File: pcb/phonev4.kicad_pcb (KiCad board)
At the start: 2 copper layers, 88.9 x 124.5 mm, 44 parts, among them J1 coin, J2 keypad, J3 display, J4 RJ9, J5 mic, J6 card_reader, J7 speaker, Q1 Si2319CDS, U2 TDA2822M

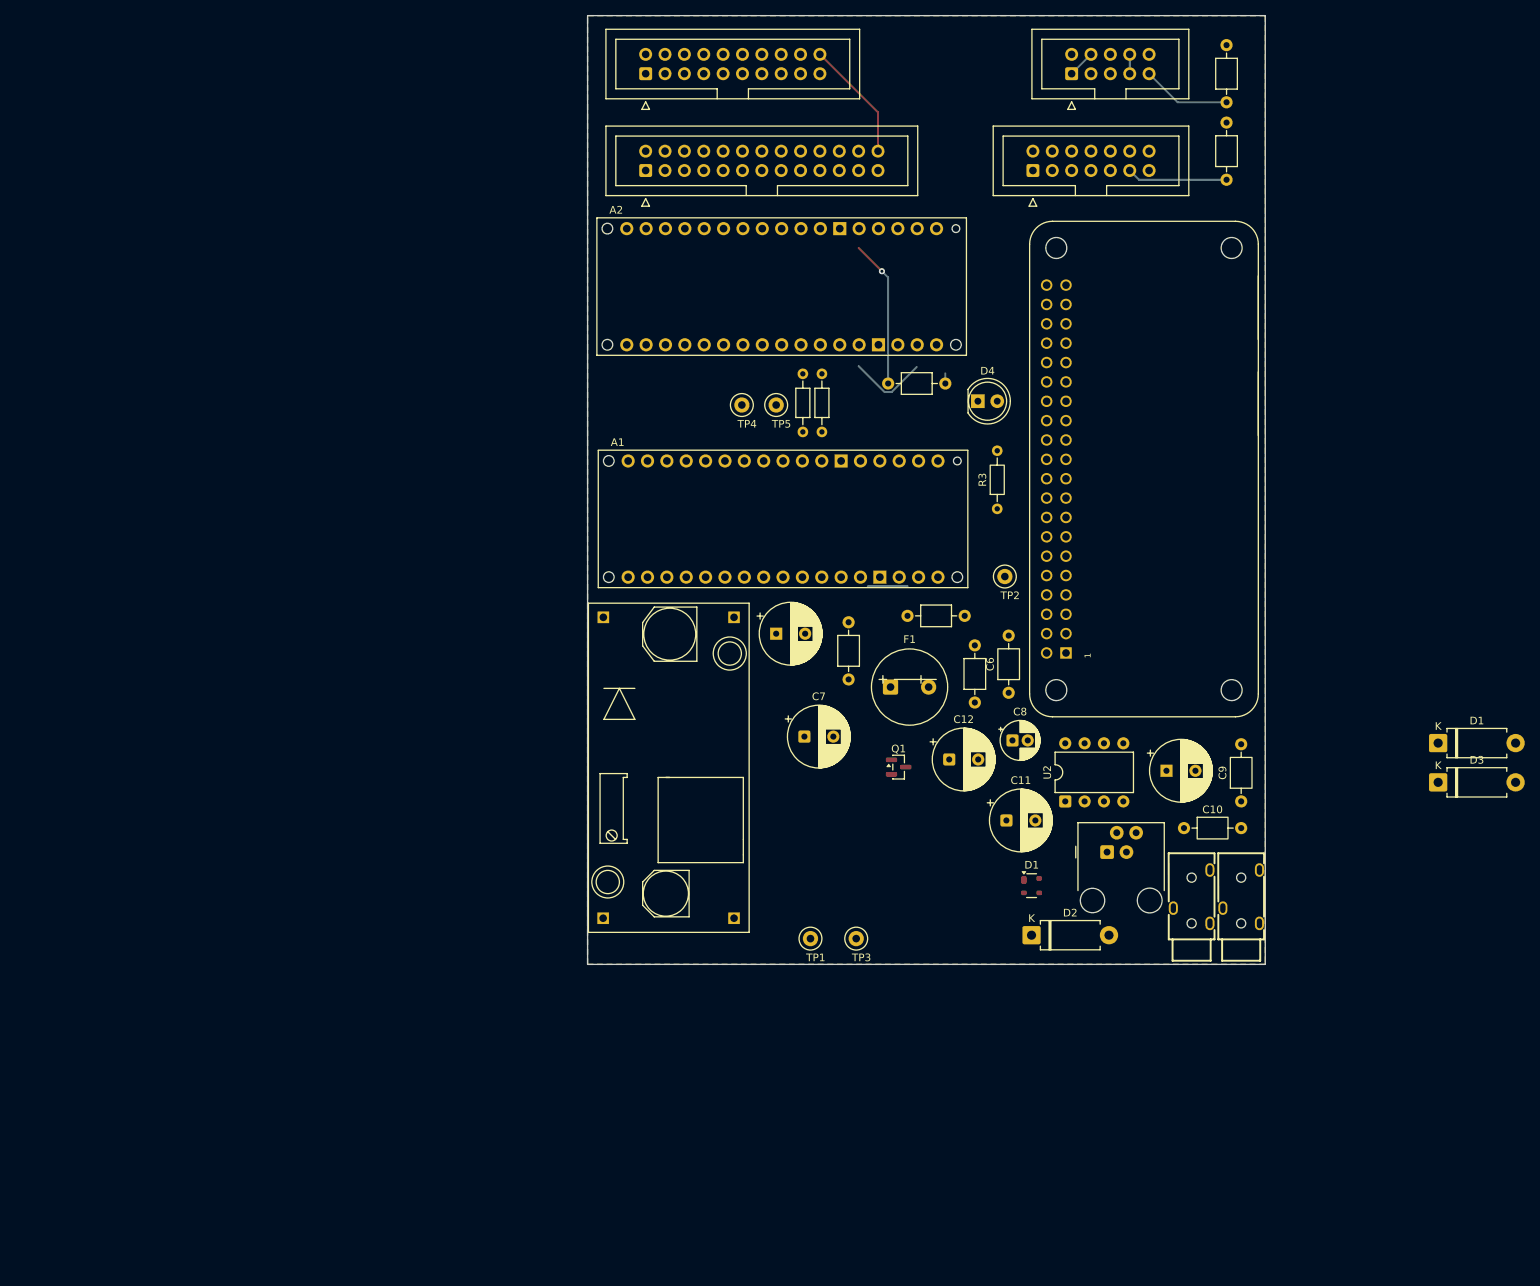
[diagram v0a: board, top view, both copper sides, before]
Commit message: pcb: phonev4 KiCad design with project footprint libraries
- Add project-local footprint libs: ADA3708, audio, PCM_arduino-library, misc_footprints
- Q1 THT: TO-220-3_Vertical_GSD for IRF9540N
- R4, R5: 1k for Pi→Arduino reset (unconnected in schematic)
- Updated fp-lib-table, BOM, README, audit script

Made-with: Cursor
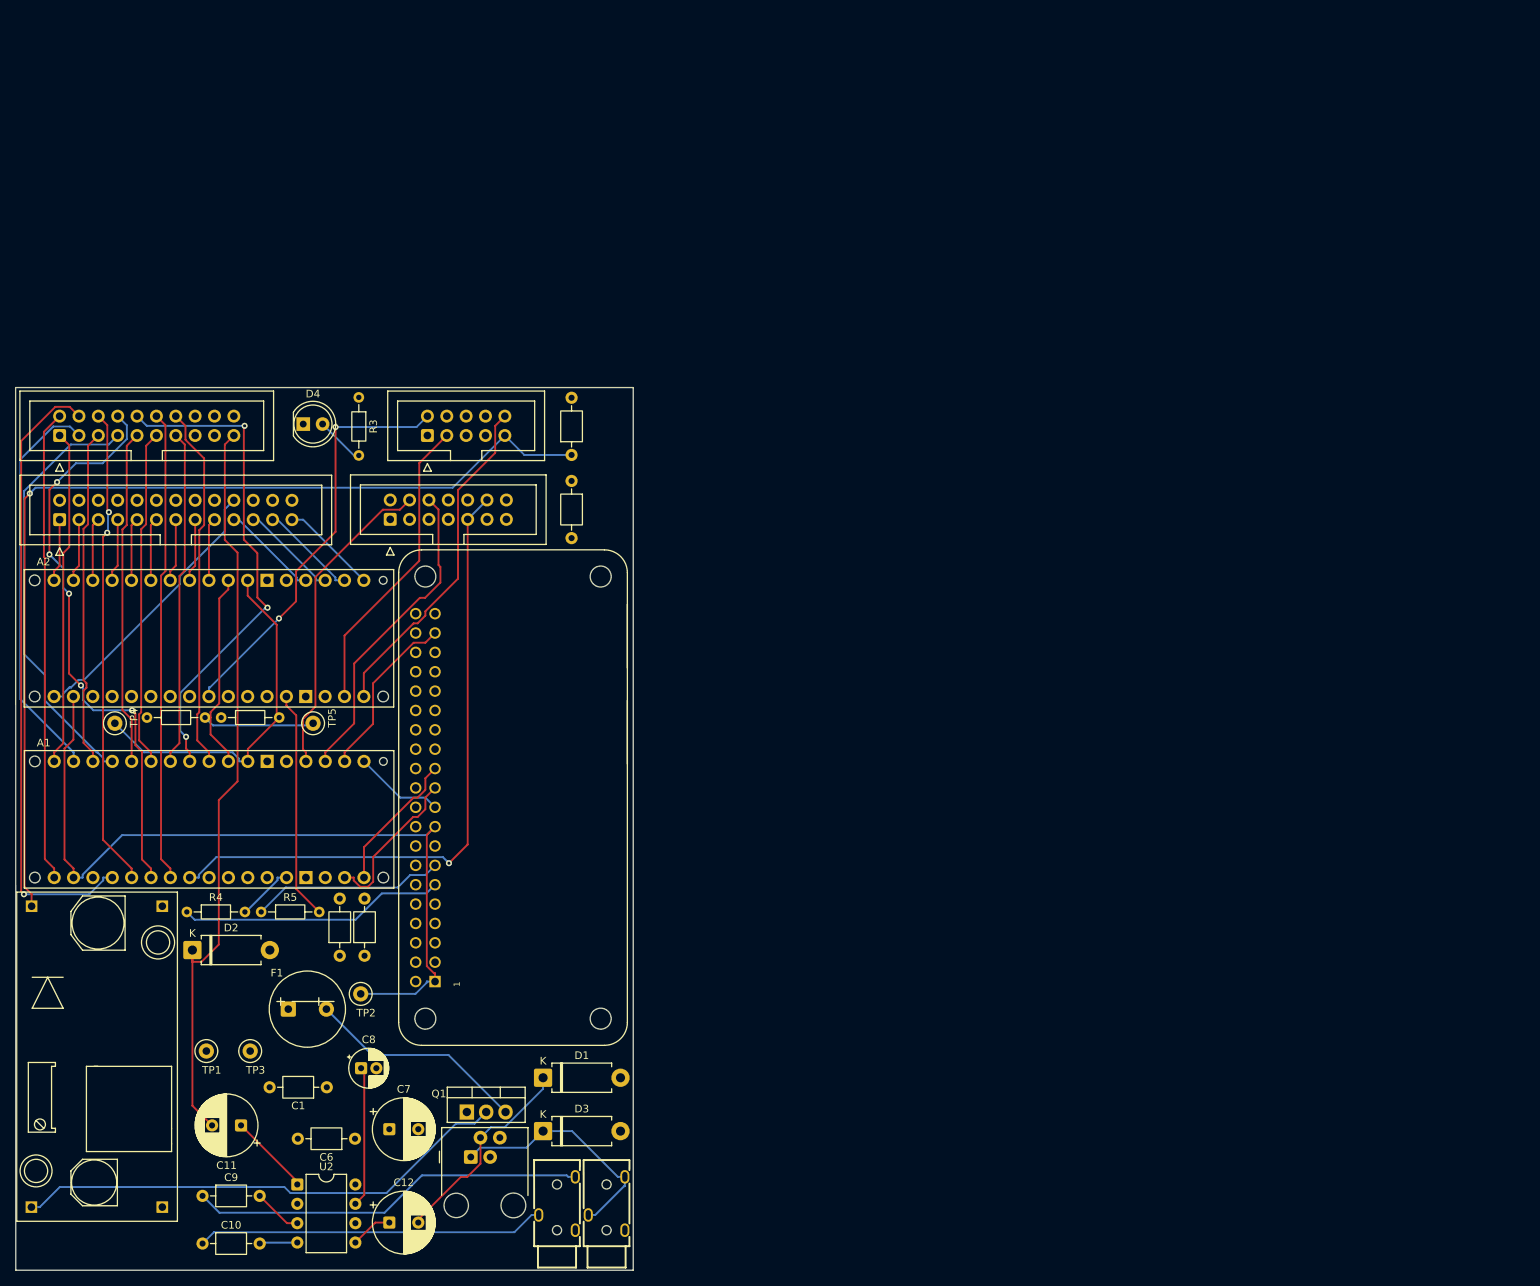
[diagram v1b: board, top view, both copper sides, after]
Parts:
- removed ? (x2): LOGO, LOGO
- removed the C1 at (158.7, 43.2)
- removed the C2 at (136.5, 76.0)
- removed the C4 at (146.0, 82.0)
- removed the D1 at (170.0, 109.0)
- added R4: 1k, Resistor_THT:R_Axial_DIN0204_L3.6mm_D1.6mm_P7.62mm_Horizontal, F.Cu at (59.2, 112.5)
- added R5: 1k, Resistor_THT:R_Axial_DIN0204_L3.6mm_D1.6mm_P7.62mm_Horizontal, F.Cu at (68.9, 112.5)
- C1: value CP_Axial_L11.0mm_D8.0mm_P15.00mm -> 0.1u; footprint Capacitor_THT:CP_Radial_D8.0mm_P3.80mm -> Capacitor_THT:C_Axial_L3.8mm_D2.6mm_P7.50mm_Horizontal
- Q1: value Si2319CDS -> IRF9540N; footprint Package_TO_SOT_SMD:SOT-23 -> footprints:TO-220-3_Vertical_GSD
- moved C9 145.7 mm to (61.2, 149.8), turned to 0 degrees
- moved C10 139.8 mm to (61.2, 156.0)
- moved D3 126.0 mm to (105.9, 141.2)
- moved D1 125.4 mm to (105.9, 134.2)
- moved C1 117.7 mm to (77.5, 135.5), turned to 180 degrees
- moved U2 112.6 mm to (73.7, 148.2), turned to 0 degrees
- moved D2 110.1 mm to (59.9, 117.5)
- moved C11 108.1 mm to (66.3, 140.5), turned to 180 degrees
- moved C6 103.8 mm to (81.2, 142.2), turned to 180 degrees
- moved TP2 100.7 mm to (82.0, 123.2)
- moved C3 97.9 mm to (109.7, 56.0)
- moved C4 97.6 mm to (109.7, 52.5)
- moved R2 97.1 mm to (54.0, 87.0), turned to 0 degrees
- moved J1 96.9 mm to (90.8, 50.0)
- moved J6 95.9 mm to (85.9, 61.0)
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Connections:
- A1 pad 3V3: unconnected-(A1-3.3V-Pad3V3) -> 3.3V
- A1 pad RST1: unconnected-(A1-RESET-PadRST1) -> RESET1
- A2 pad 3V3: unconnected-(A2-3.3V-Pad3V3) -> 3.3V
- A2 pad RST1: unconnected-(A2-RESET-PadRST1) -> RESET2
- A3 pad 1: Net-(A3-3V3[1]) -> 3.3V
- A3 pad 11: unconnected-(A3-GPIO17/GEN0-Pad11) -> PI_RESET1
- A3 pad 13: unconnected-(A3-GPIO27/GEN2-Pad13) -> PI_RESET2
- A3 pad 17: unconnected-(A3-3V3[2]-Pad17) -> 3.3V
- C1 pad 1: Net-(U2-BYPASS) -> 5V_MAIN
- C1 pad 2: gnd -> GND
- C6 pad 2: Net-(U2-V+) -> GND
- C7 pad 2: Net-(U2-V+) -> GND
- TP2 pad 1: Net-(A3-3V3[1]) -> 3.3V
- U2 pad 6: Net-(U2-V+) -> 5V_MAIN
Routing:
- net 12V_COIN: track 11.7 -> 130.1 mm, vias 0 -> 1
- net 3.3V: track 0.00 -> 106.9 mm
- net speaker_front+: track 0.00 -> 99.0 mm
- net mag_cls: track 0.00 -> 85.4 mm, vias 0 -> 1
- net key_col_5: track 0.00 -> 82.3 mm, vias 0 -> 1
- net key_col_7: track 0.00 -> 75.8 mm, vias 0 -> 5
- net BOOST_IN+: track 0.00 -> 65.5 mm
- net key_hook_up: track 0.00 -> 65.4 mm, vias 0 -> 3
- net key_col_6: track 0.00 -> 63.0 mm, vias 0 -> 2
- net key_col_4: track 0.00 -> 61.9 mm
- net key_hook_common: track 0.00 -> 61.8 mm
- net key_row_1: track 0.00 -> 56.3 mm
- net coin_tx: track 0.00 -> 54.9 mm, vias 0 -> 2
- net key_col_2: track 0.00 -> 52.5 mm
- net speaker_front_pre+: track 0.00 -> 51.9 mm
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- added copper zone on In2.Cu, net 5V_MAIN
- added copper zone on In1.Cu, net GND
- removed copper zone on B.Cu, net 5V_MAIN
- removed copper zone on F.Cu, net GND
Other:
- board size 88.9 x 124.5 mm -> 81 x 115.8 mm
- copper layers 2 -> 4
